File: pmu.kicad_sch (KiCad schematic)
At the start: 21 parts, among them J4 Battery, Q4 BSS138, Q5 BSS84, SW1 POWER ON, U3 MAX1555, U4 TPS63030DSK

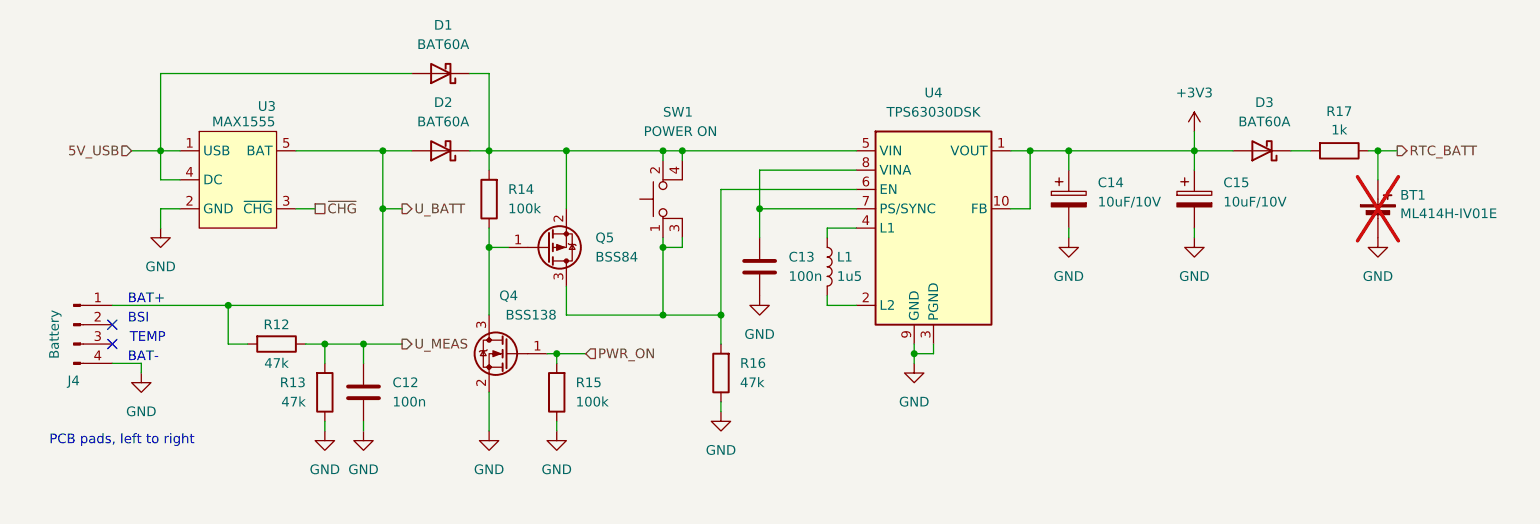
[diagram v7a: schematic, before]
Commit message: mayhem
- removed sd card slot
- started pcb design
- added nice 3310 photos
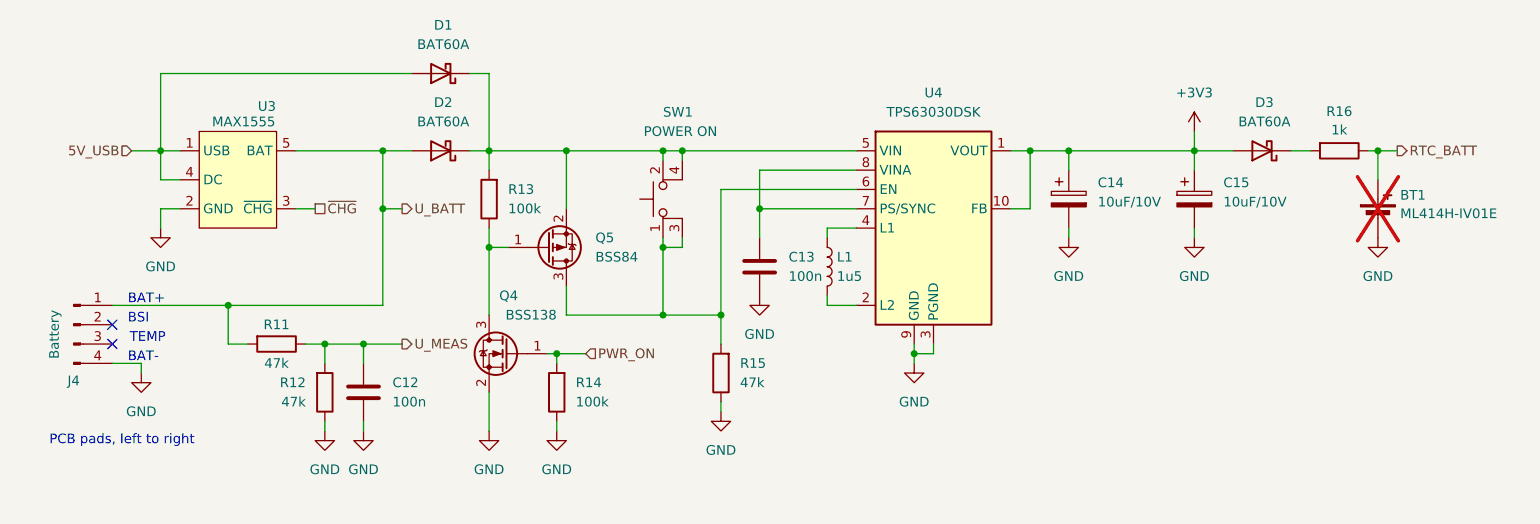
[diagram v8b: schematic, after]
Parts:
- J4: footprint (none) -> Parts:3310_batt
- renumbered R12 to R11, R13 to R12, R14 to R13, R15 to R14, R16 to R15, R17 to R16
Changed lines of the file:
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@@
 		(dnp no)
 		(fields_autoplaced yes)
-		(property "Reference" "#PWR040"
+		(property "Reference" "#PWR047"
 			(at 201.93 101.6 0)
 			(effects
@@
 			(project "M17_3310"
 				(path "/8d65c5ef-7a02-4454-aee5-ab9c49e4aeab/69b4d1b1-805b-4c7a-b583-ffe559937ec6"
-					(reference "#PWR040")
+					(reference "#PWR047")
 					(unit 1)
 				)
@@
 		(dnp no)
 		(fields_autoplaced yes)
-		(property "Reference" "R15"
+		(property "Reference" "R14"
 			(at 120.6104 114.2999 0)
 			(effects
@@
 			(project "M17_3310"
 				(path "/8d65c5ef-7a02-4454-aee5-ab9c49e4aeab/69b4d1b1-805b-4c7a-b583-ffe559937ec6"
-					(reference "R15")
+					(reference "R14")
 					(unit 1)
 				)
@@
 		(dnp no)
 		(fields_autoplaced yes)
-		(property "Reference" "#PWR031"
+		(property "Reference" "#PWR038"
 			(at 87.63 127 0)
 			(effects
@@
 			(project "M17_3310"
 				(path "/8d65c5ef-7a02-4454-aee5-ab9c49e4aeab/69b4d1b1-805b-4c7a-b583-ffe559937ec6"
-					(reference "#PWR031")
+					(reference "#PWR038")
 					(unit 1)
 				)
@@
 		(on_board yes)
 		(dnp no)
-		(property "Reference" "R13"
+		(property "Reference" "R12"
 			(at 85.1296 114.2999 0)
 			(effects
@@
 			(project "M17_3310"
 				(path "/8d65c5ef-7a02-4454-aee5-ab9c49e4aeab/69b4d1b1-805b-4c7a-b583-ffe559937ec6"
-					(reference "R13")
+					(reference "R12")
 					(unit 1)
 				)
@@
 		(dnp no)
 		(fields_autoplaced yes)
-		(property "Reference" "#PWR041"
+		(property "Reference" "#PWR048"
 			(at 226.06 101.6 0)
 			(effects
@@
 			(project "M17_3310"
 				(path "/8d65c5ef-7a02-4454-aee5-ab9c49e4aeab/69b4d1b1-805b-4c7a-b583-ffe559937ec6"
-					(reference "#PWR041")
+					(reference "#PWR048")
 					(unit 1)
 				)
@@
 		(dnp no)
 		(fields_autoplaced yes)
-		(property "Reference" "R16"
+		(property "Reference" "R15"
 			(at 142.2004 111.7599 0)
 			(effects
@@
 			(project "M17_3310"
 				(path "/8d65c5ef-7a02-4454-aee5-ab9c49e4aeab/69b4d1b1-805b-4c7a-b583-ffe559937ec6"
-					(reference "R16")
+					(reference "R15")
 					(unit 1)
 				)
@@
 			)
 		)
-		(property "Footprint" ""
+		(property "Footprint" "Parts:3310_batt"
 			(at 54.61 106.68 0)
 			(effects
@@
 		(dnp no)
 		(fields_autoplaced yes)
-		(property "Reference" "#PWR033"
+		(property "Reference" "#PWR040"
 			(at 109.22 127 0)
 			(effects
@@
 			(project "M17_3310"
 				(path "/8d65c5ef-7a02-4454-aee5-ab9c49e4aeab/69b4d1b1-805b-4c7a-b583-ffe559937ec6"
-					(reference "#PWR033")
+					(reference "#PWR040")
 					(unit 1)
 				)
@@
 		(dnp no)
 		(fields_autoplaced yes)
-		(property "Reference" "#PWR036"
+		(property "Reference" "#PWR043"
 			(at 144.78 109.22 0)
 			(effects
@@
 			(project "M17_3310"
 				(path "/8d65c5ef-7a02-4454-aee5-ab9c49e4aeab/69b4d1b1-805b-4c7a-b583-ffe559937ec6"
-					(reference "#PWR036")
+					(reference "#PWR043")
 					(unit 1)
 				)
@@
 		(dnp no)
 		(fields_autoplaced yes)
-		(property "Reference" "#PWR029"
+		(property "Reference" "#PWR036"
 			(at 63.5 119.38 0)
 			(effects
@@
 			(project "M17_3310"
 				(path "/8d65c5ef-7a02-4454-aee5-ab9c49e4aeab/69b4d1b1-805b-4c7a-b583-ffe559937ec6"
-					(reference "#PWR029")
+					(reference "#PWR036")
 					(unit 1)
 				)
@@
 		(dnp no)
 		(fields_autoplaced yes)
-		(property "Reference" "#PWR037"
+		(property "Reference" "#PWR044"
 			(at 165.1 118.11 0)
 			(effects
@@
 			(project "M17_3310"
 				(path "/8d65c5ef-7a02-4454-aee5-ab9c49e4aeab/69b4d1b1-805b-4c7a-b583-ffe559937ec6"
-					(reference "#PWR037")
+					(reference "#PWR044")
 					(unit 1)
 				)
@@
 		(dnp no)
 		(fields_autoplaced yes)
-		(property "Reference" "R14"
+		(property "Reference" "R13"
 			(at 111.7204 88.8999 0)
 			(effects
@@
 			(project "M17_3310"
 				(path "/8d65c5ef-7a02-4454-aee5-ab9c49e4aeab/69b4d1b1-805b-4c7a-b583-ffe559937ec6"
-					(reference "R14")
+					(reference "R13")
 					(unit 1)
 				)
@@
 		(dnp no)
 		(fields_autoplaced yes)
-		(property "Reference" "#PWR032"
+		(property "Reference" "#PWR039"
 			(at 92.71 127 0)
 			(effects
@@
 			(project "M17_3310"
 				(path "/8d65c5ef-7a02-4454-aee5-ab9c49e4aeab/69b4d1b1-805b-4c7a-b583-ffe559937ec6"
-					(reference "#PWR032")
+					(reference "#PWR039")
 					(unit 1)
 				)
@@
 		(dnp no)
 		(fields_autoplaced yes)
-		(property "Reference" "#PWR035"
+		(property "Reference" "#PWR042"
 			(at 139.7 124.46 0)
 			(effects
@@
 			(project "M17_3310"
 				(path "/8d65c5ef-7a02-4454-aee5-ab9c49e4aeab/69b4d1b1-805b-4c7a-b583-ffe559937ec6"
-					(reference "#PWR035")
+					(reference "#PWR042")
 					(unit 1)
 				)
@@
 		(dnp no)
 		(fields_autoplaced yes)
-		(property "Reference" "#PWR038"
+		(property "Reference" "#PWR045"
 			(at 185.42 101.6 0)
 			(effects
@@
 			(project "M17_3310"
 				(path "/8d65c5ef-7a02-4454-aee5-ab9c49e4aeab/69b4d1b1-805b-4c7a-b583-ffe559937ec6"
-					(reference "#PWR038")
+					(reference "#PWR045")
 					(unit 1)
 				)
@@
 		(dnp no)
 		(fields_autoplaced yes)
-		(property "Reference" "#PWR039"
+		(property "Reference" "#PWR046"
 			(at 201.93 85.09 0)
 			(effects
@@
 			(project ""
 				(path "/8d65c5ef-7a02-4454-aee5-ab9c49e4aeab/69b4d1b1-805b-4c7a-b583-ffe559937ec6"
-					(reference "#PWR039")
+					(reference "#PWR046")
 					(unit 1)
 				)
@@
 		(on_board yes)
 		(dnp no)
-		(property "Reference" "R12"
+		(property "Reference" "R11"
 			(at 81.28 106.68 90)
 			(effects
@@
 			(project "M17_3310"
 				(path "/8d65c5ef-7a02-4454-aee5-ab9c49e4aeab/69b4d1b1-805b-4c7a-b583-ffe559937ec6"
-					(reference "R12")
+					(reference "R11")
 					(unit 1)
 				)
@@
 		(dnp no)
 		(fields_autoplaced yes)
-		(property "Reference" "R17"
+		(property "Reference" "R16"
 			(at 220.98 78.6595 90)
 			(effects
@@
 			(project "M17_3310"
 				(path "/8d65c5ef-7a02-4454-aee5-ab9c49e4aeab/69b4d1b1-805b-4c7a-b583-ffe559937ec6"
-					(reference "R17")
+					(reference "R16")
 					(unit 1)
 				)
@@
 		(dnp no)
 		(fields_autoplaced yes)
-		(property "Reference" "#PWR030"
+		(property "Reference" "#PWR037"
 			(at 66.04 100.33 0)
 			(effects
@@
 			(project ""
 				(path "/8d65c5ef-7a02-4454-aee5-ab9c49e4aeab/69b4d1b1-805b-4c7a-b583-ffe559937ec6"
-					(reference "#PWR030")
+					(reference "#PWR037")
 					(unit 1)
 				)
@@
 		(dnp no)
 		(fields_autoplaced yes)
-		(property "Reference" "#PWR034"
+		(property "Reference" "#PWR041"
 			(at 118.11 127 0)
 			(effects
@@
 			(project "M17_3310"
 				(path "/8d65c5ef-7a02-4454-aee5-ab9c49e4aeab/69b4d1b1-805b-4c7a-b583-ffe559937ec6"
-					(reference "#PWR034")
-					(unit 1)
-				)
+					(reference "#PWR041")
+					(unit 1)
+				)
